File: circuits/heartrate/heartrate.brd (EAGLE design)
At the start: 24.9 x 17 mm, 21 parts

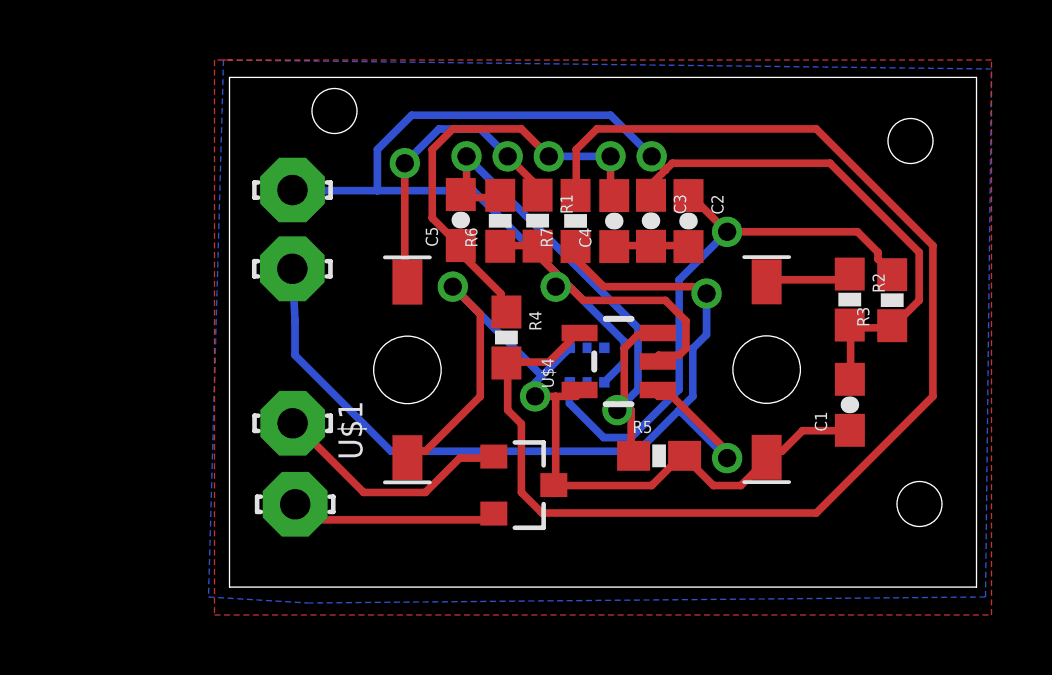
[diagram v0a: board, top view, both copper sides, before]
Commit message: finished new heart rate sensor layout
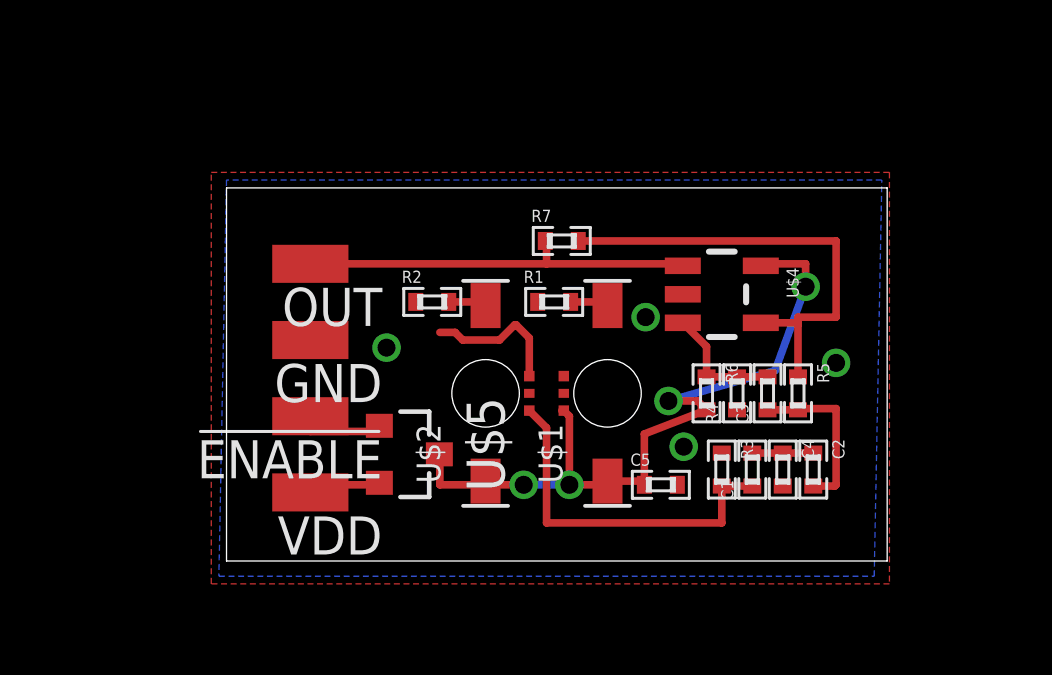
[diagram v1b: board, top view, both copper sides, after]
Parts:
- !ENABLE, GND, OUT, VDD: value LSP10 -> (none); device solpad:LSP10 -> wirepad:SMD1,27-2,54
- C1: value 2.2uF -> 4.7uF; device SparkFun-Passives:0603-CAP -> standardparts:0402
- C2, C4: value 4.7 uF -> 4.7uF; device SparkFun-Capacitors:0603-CAP -> standardparts:0402
- C3: value 4.7 uF -> 2.2uF; device SparkFun-Capacitors:0603-CAP -> standardparts:0402
- C5: value 2.2 uF -> 2.2uF; device SparkFun-Capacitors:0603-CAP -> standardparts:0402
- R1, R2, R3, R6, R7: device SparkFun-Passives:0603-RES -> standardparts:0402
- R4: value 10k -> 100k; device SparkFun-Passives:0603-RES -> standardparts:0402
- R5: value 100k -> 10k; device SparkFun-Passives:0603-RES -> standardparts:0402
- moved R2 13.9 mm to (6.86, 8.64), turned to 0 degrees
- moved C5 11.1 mm to (14.5, 2.54), turned to 0 degrees
- moved C4 10.0 mm to (18.5, 3.05), turned to 270 degrees
- moved U$2 9.40 mm to (8.64, 5.59)
- moved C2 9.27 mm to (19.6, 3.05)
- moved R6 8.97 mm to (16.0, 5.59), turned to 270 degrees
- moved R3 8.01 mm to (16.5, 3.05), turned to 270 degrees
- moved R4 7.91 mm to (17.0, 5.59), turned to 90 degrees
- moved C3 6.94 mm to (18.0, 5.59), turned to 90 degrees
- moved U$1 6.72 mm to (12.7, 5.59)
- moved R5 5.08 mm to (19.1, 5.59), turned to 270 degrees
- moved GND 5.03 mm to (2.79, 7.37), turned to 90 degrees
- moved U$4 4.11 mm to (16.5, 8.89), turned to 270 degrees
- moved U$5 3.95 mm to (6.10, 3.56)
- moved C1 3.90 mm to (17.5, 3.05)
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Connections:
- removed net GND-ISO: C1.2, C3.1, GND.MP, R1.2, R2.2, R3.1, R6.1, U$3.GND, U$4.VSS
- new net GND: C4.2, C5.2, GND.1, R1.1, R2.1, R3.1, R4.1, U$3.GND, U$4.VSS
- net N$1: now also R1.2; no longer R1.1
- net N$10: now also C3.2, R4.2, R6.1; no longer C5.2, R5.1, R6.2
- net N$12: now also R5.1; no longer R4.2
- net N$2: now also VDD.1; no longer VDD.MP
- net N$3: now also !ENABLE.1; no longer !ENABLE.MP
- net N$4: now also R2.2; no longer R2.1
- net N$5: now also C1.1; no longer C2.1
- net N$6: now also C1.2, C2.1; no longer C2.2, C3.2
- net N$7: now also C2.2, C3.1, R5.2; no longer C4.2, C5.1, R4.1
- net OUT: now also OUT.1; no longer OUT.MP
- net VDD: now also C5.1, R6.2; no longer C1.1, R5.2
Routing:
- net GND-ISO: track 54.2 -> 0.00 mm, vias 2 -> 0
- net N$12: track 43.3 -> 15.6 mm
- net OUT: track 32.8 -> 13.2 mm, vias 2 -> 0
- net N$10: track 19.2 -> 4.16 mm, vias 2 -> 0
- net VDD: track 29.8 -> 16.8 mm, vias 2 -> 0
- net N$7: track 14.4 -> 5.62 mm, vias 2 -> 0
- net N$1: track 9.98 -> 1.35 mm, vias 2 -> 0
- net N$5: track 19.4 -> 12.1 mm, vias 1 -> 0
- net N$17: track 0.00 -> 6.67 mm, vias 0 -> 2
- net GND: track 0.00 -> 5.51 mm, vias 0 -> 4
- net N$3: track 8.13 -> 3.00 mm
- net N$2: track 7.04 -> 3.13 mm
- net N$4: track 2.88 -> 1.35 mm
- net N$11: track 0.00 -> 1.52 mm, vias 0 -> 2
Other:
- board size 24.9 x 17 mm -> 22 x 12.4 mm
